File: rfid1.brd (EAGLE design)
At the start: 63.5 x 84.5 mm, 71 parts, among them IC1 EM4095, J1 AVR_SPI_PRG_6PTH, U1 MCP73831, U2 TPS61200, X2 USB-MICROB, Y2 RESONATORSMD

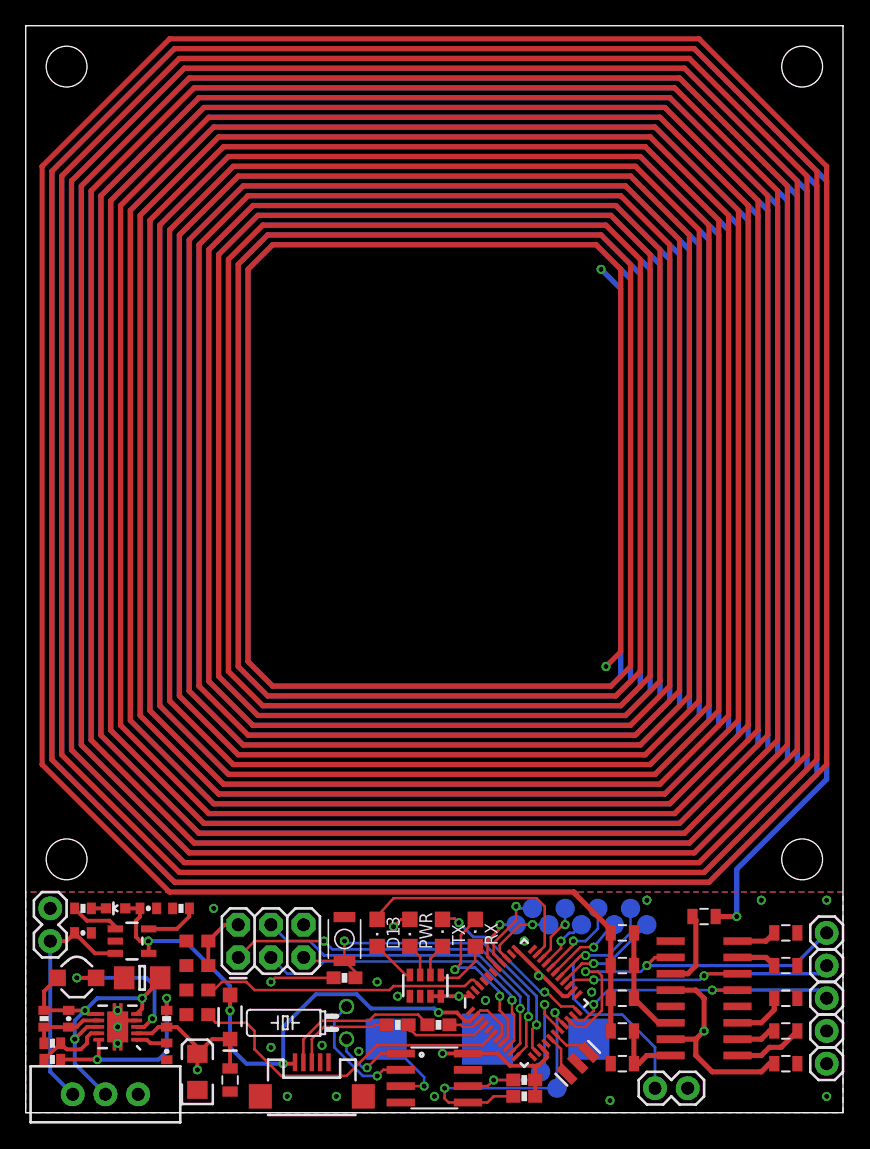
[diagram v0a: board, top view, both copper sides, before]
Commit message: Updated part sizes and added acces pads for unused avr pins.  Added silk labels and free area.  Revision sent for manufacturing 6/4/12
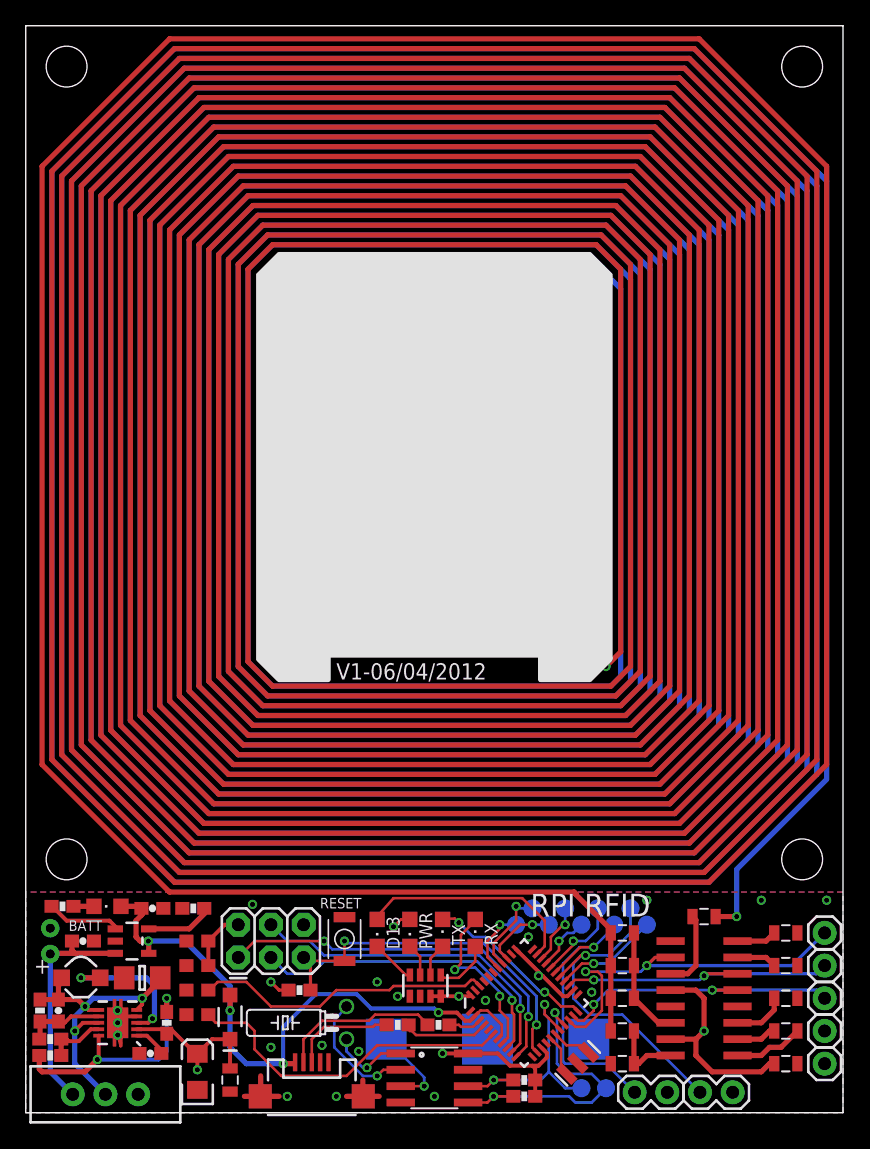
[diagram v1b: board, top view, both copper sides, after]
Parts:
- removed D4: red, SparkFun:LED-0603
- added CHARGE: RED, led:CHIPLED_0805
- added LIGHT: (no value), SparkFun-Connectors:1X02
- C11, C12, C14, C15: device SparkFun:0402-CAP -> SparkFun:0603-CAP
- LIPO: device SparkFun-Connectors:1X02 -> SparkFun-Connectors:JST-2-PTH-NS
- R10, R11, R3, R4, R5, R9: device SparkFun:0402-RES -> SparkFun:0603-RES
- TP1, TP13, TP14, TP2, TP3, TP4, TP5, TP6, TP7, TP8, TP9: value PTR1TP15R -> PTR1TP14R; device testpad:TP15R -> testpad:TP14R
- moved TP13 3.81 mm to (45.1, 1.27)
- moved R7 3.62 mm to (21.3, 8.89)
- moved BUZZER 3.51 mm to (52.4, 0.95)
- moved TP14 3.42 mm to (43.2, 1.27)
- moved R9 1.60 mm to (2.86, 15.4)
- moved C15 1.28 mm to (9.68, 3.97), turned to 180 degrees
- moved C14 1.02 mm to (2.54, 7.30)
- moved R5 0.95 mm to (13.0, 15.2)
- moved R3 0.71 mm to (1.11, 7.30)
- moved C12 0.64 mm to (4.45, 12.7)
- moved R10 0.35 mm to (1.91, 3.81), turned to 180 degrees
- moved R4 0.35 mm to (1.91, 5.08)
- moved R11 0.32 mm to (11.0, 6.35)
- moved L1 0.32 mm to (4.29, 9.84)
- moved U2 0.32 mm to (7.14, 6.35)
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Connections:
- net D8: now also LIGHT.1
- net GND: now also LIGHT.2
- net N$2: now also CHARGE.C; no longer D4.C
- net VBUS: now also CHARGE.A; no longer D4.A
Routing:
- net D8: track 6.21 -> 23.3 mm
- net GND: track 2.37 -> 8.44 mm, vias 19 -> 17
- net SCL: track 15.4 -> 19.6 mm
- net FB: track 15.2 -> 18.8 mm
- net VCC: track 62.4 -> 59.2 mm
- net N$14: track 4.20 -> 6.05 mm
- net D6: track 23.8 -> 25.6 mm
- net GND1: track 5.80 -> 4.63 mm
- net RST: track 27.8 -> 28.9 mm
- net REF: track 22.1 -> 23.2 mm
- net N$11: track 5.45 -> 6.47 mm
- net UVLO: track 5.71 -> 6.65 mm
- net BATT_IN: track 25.8 -> 24.9 mm
- net VBATT: track 18.6 -> 17.8 mm
- net D13: track 18.1 -> 17.4 mm
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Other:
- board text added: "+"
- board text added: "5V"
- board text added: "A0"
- board text added: "A1"
- board text added: "A2"
- board text added: "BATT"
- board text added: "BUZZ"
- board text added: "CLK"
- board text added: "D10"
- board text added: "D12"
- board text added: "D5"
- board text added: "D6"
- board text added: "D8"
- board text added: "D9"
- board text added: "DATA"
- board text added: "EN"
- board text added: "GND"
- board text added: "LIGHT"
- board text added: "OFF"
- board text added: "ON"
- board text added: "RESET"
- board text added: "RPI RFID"
- board text added: "SCL"
- board text added: "SDA"
- board text added: "V1-06/04/2012"
